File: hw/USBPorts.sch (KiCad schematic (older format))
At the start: 17 parts, among them J3 Conn_01x04, J4 USB_A, J5 Conn_01x04, J6 USB_A, J7 USB_A, J8 USB_A, U10 FSUSB31, U3 USB2517, U5 FSUSB31, U6 MIC2026-2BM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

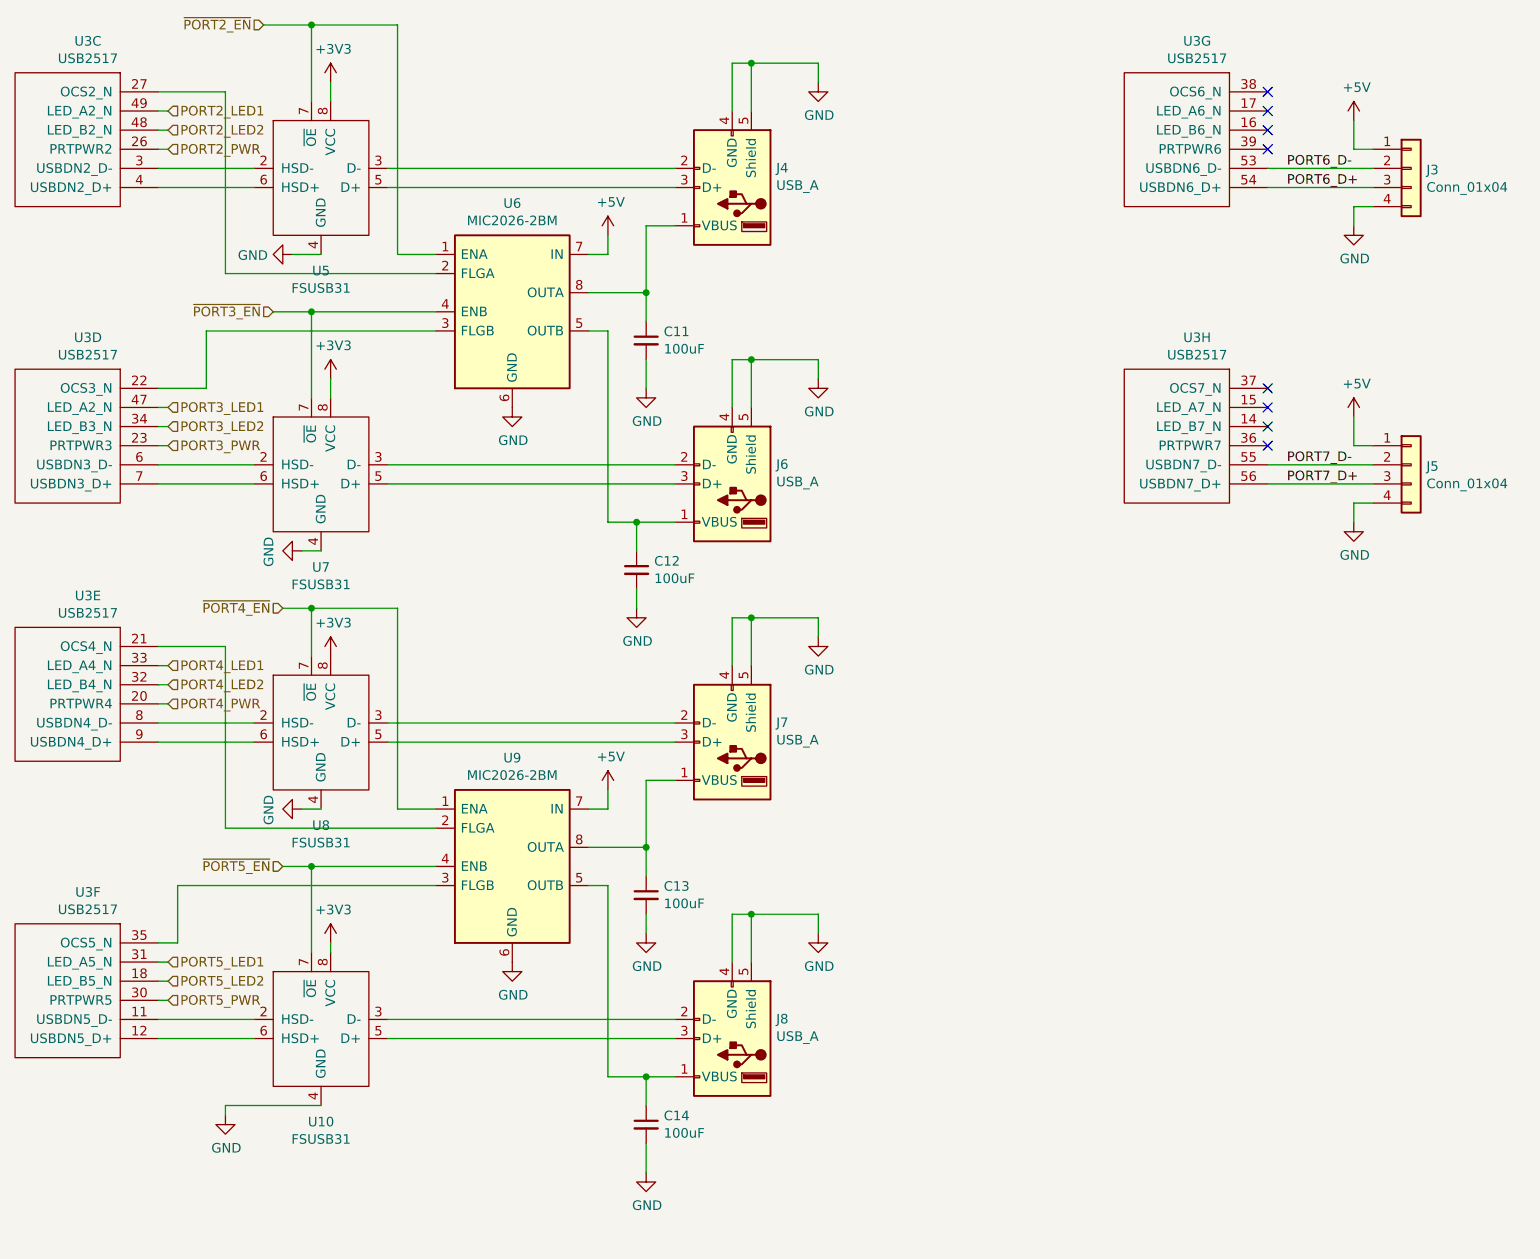
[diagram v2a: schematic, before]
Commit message: Add most footprints, switch to usb c
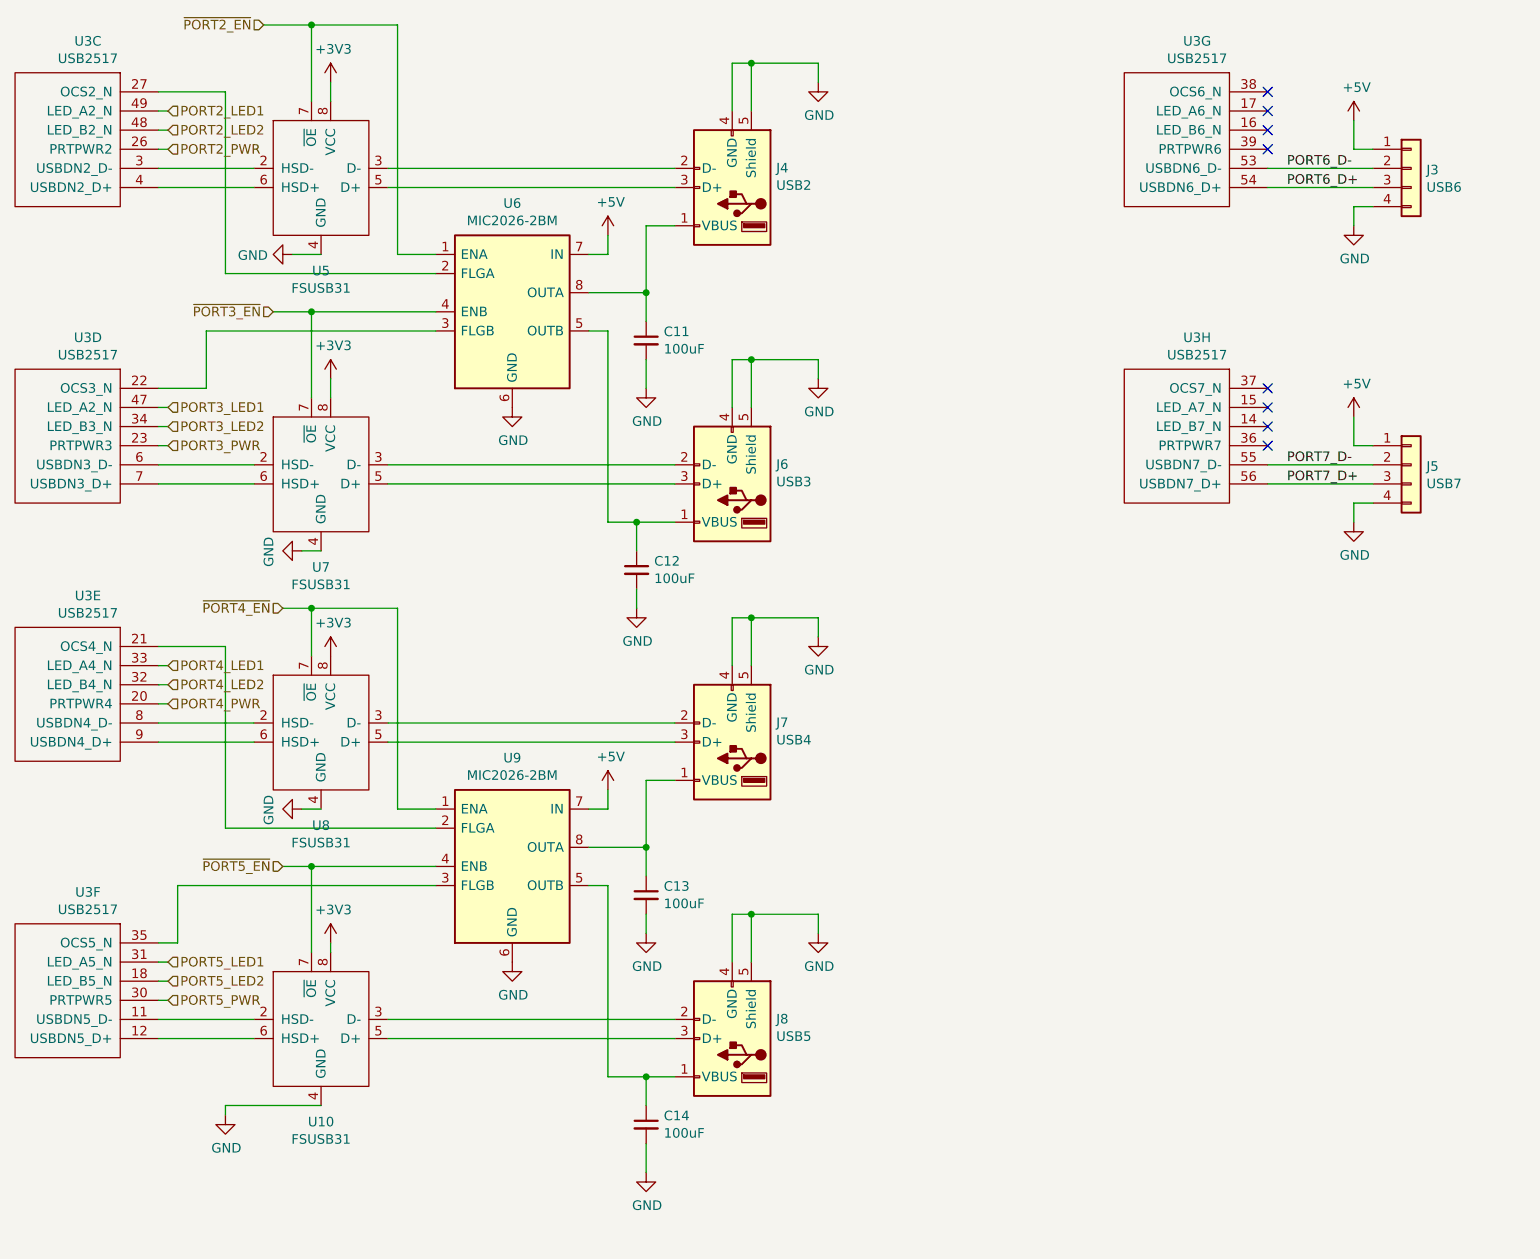
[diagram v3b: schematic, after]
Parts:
- C11, C12, C13, C14: footprint (none) -> Capacitor_SMD:C_0603_1608Metric
- J3: value Conn_01x04 -> USB6; footprint (none) -> Connector_PinHeader_2.54mm:PinHeader_1x04_P2.54mm_Vertical
- J4: value USB_A -> USB2; footprint (none) -> USB_A_Female_Vertical:USB_A_Female_Vertical
- J5: value Conn_01x04 -> USB7; footprint (none) -> Connector_PinHeader_2.54mm:PinHeader_1x04_P2.54mm_Vertical
- J6: value USB_A -> USB3; footprint (none) -> USB_A_Female_Vertical:USB_A_Female_Vertical
- J7: value USB_A -> USB4; footprint (none) -> USB_A_Female_Vertical:USB_A_Female_Vertical
- J8: value USB_A -> USB5; footprint (none) -> USB_A_Female_Vertical:USB_A_Female_Vertical
- U3: footprint (none) -> Package_DFN_QFN:QFN-64-1EP_9x9mm_P0.5mm_EP4.7x4.7mm_ThermalVias
- U6, U9: footprint (none) -> Package_SO:SOIC-8_3.9x4.9mm_P1.27mm
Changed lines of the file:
@@
 F 0 "U3" H 1531 2065 50  0000 C CNN
 F 1 "USB2517" H 1531 1974 50  0000 C CNN
-F 2 "" H 2550 3350 50  0001 C CNN
+F 2 "Package_DFN_QFN:QFN-64-1EP_9x9mm_P0.5mm_EP4.7x4.7mm_ThermalVias" H 2550 3350 50  0001 C CNN
 F 3 "" H 2550 3350 50  0001 C CNN
 	3    1450 1550
@@
 F 0 "U3" H 1531 3615 50  0000 C CNN
 F 1 "USB2517" H 1531 3524 50  0000 C CNN
-F 2 "" H 2550 4900 50  0001 C CNN
+F 2 "Package_DFN_QFN:QFN-64-1EP_9x9mm_P0.5mm_EP4.7x4.7mm_ThermalVias" H 2550 4900 50  0001 C CNN
 F 3 "" H 2550 4900 50  0001 C CNN
 	4    1450 3100
@@
 F 0 "U3" H 1531 4965 50  0000 C CNN
 F 1 "USB2517" H 1531 4874 50  0000 C CNN
-F 2 "" H 2550 6250 50  0001 C CNN
+F 2 "Package_DFN_QFN:QFN-64-1EP_9x9mm_P0.5mm_EP4.7x4.7mm_ThermalVias" H 2550 6250 50  0001 C CNN
 F 3 "" H 2550 6250 50  0001 C CNN
 	5    1450 4450
@@
 F 0 "U3" H 1531 6515 50  0000 C CNN
 F 1 "USB2517" H 1531 6424 50  0000 C CNN
-F 2 "" H 2550 7800 50  0001 C CNN
+F 2 "Package_DFN_QFN:QFN-64-1EP_9x9mm_P0.5mm_EP4.7x4.7mm_ThermalVias" H 2550 7800 50  0001 C CNN
 F 3 "" H 2550 7800 50  0001 C CNN
 	6    1450 6000
@@
 F 0 "U3" H 7331 2065 50  0000 C CNN
 F 1 "USB2517" H 7331 1974 50  0000 C CNN
-F 2 "" H 8350 3350 50  0001 C CNN
+F 2 "Package_DFN_QFN:QFN-64-1EP_9x9mm_P0.5mm_EP4.7x4.7mm_ThermalVias" H 8350 3350 50  0001 C CNN
 F 3 "" H 8350 3350 50  0001 C CNN
 	7    7250 1550
@@
 F 0 "U3" H 7331 3615 50  0000 C CNN
 F 1 "USB2517" H 7331 3524 50  0000 C CNN
-F 2 "" H 8350 4900 50  0001 C CNN
+F 2 "Package_DFN_QFN:QFN-64-1EP_9x9mm_P0.5mm_EP4.7x4.7mm_ThermalVias" H 8350 4900 50  0001 C CNN
 F 3 "" H 8350 4900 50  0001 C CNN
 	8    7250 3100
@@
 F 0 "U6" H 3750 3017 50  0000 C CNN
 F 1 "MIC2026-2BM" H 3750 2926 50  0000 C CNN
-F 2 "" H 3750 2450 50  0001 C CNN
+F 2 "Package_SO:SOIC-8_3.9x4.9mm_P1.27mm" H 3750 2450 50  0001 C CNN
 F 3 "http://www.micrel.com/_PDF/mic2026.pdf" H 3750 2450 50  0001 C CNN
 	1    3750 2450
@@
 P 4900 1800
 F 0 "J4" H 4670 1698 50  0000 R CNN
-F 1 "USB_A" H 4670 1789 50  0000 R CNN
-F 2 "" H 5050 1750 50  0001 C CNN
+F 1 "USB2" H 4670 1789 50  0000 R CNN
+F 2 "USB_A_Female_Vertical:USB_A_Female_Vertical" H 5050 1750 50  0001 C CNN
 F 3 " ~" H 5050 1750 50  0001 C CNN
 	1    4900 1800
@@
 P 4900 3350
 F 0 "J6" H 4670 3248 50  0000 R CNN
-F 1 "USB_A" H 4670 3339 50  0000 R CNN
-F 2 "" H 5050 3300 50  0001 C CNN
+F 1 "USB3" H 4670 3339 50  0000 R CNN
+F 2 "USB_A_Female_Vertical:USB_A_Female_Vertical" H 5050 3300 50  0001 C CNN
 F 3 " ~" H 5050 3300 50  0001 C CNN
 	1    4900 3350
@@
 F 0 "U9" H 3750 5917 50  0000 C CNN
 F 1 "MIC2026-2BM" H 3750 5826 50  0000 C CNN
-F 2 "" H 3750 5350 50  0001 C CNN
+F 2 "Package_SO:SOIC-8_3.9x4.9mm_P1.27mm" H 3750 5350 50  0001 C CNN
 F 3 "http://www.micrel.com/_PDF/mic2026.pdf" H 3750 5350 50  0001 C CNN
 	1    3750 5350
@@
 P 4900 4700
 F 0 "J7" H 4670 4598 50  0000 R CNN
-F 1 "USB_A" H 4670 4689 50  0000 R CNN
-F 2 "" H 5050 4650 50  0001 C CNN
+F 1 "USB4" H 4670 4689 50  0000 R CNN
+F 2 "USB_A_Female_Vertical:USB_A_Female_Vertical" H 5050 4650 50  0001 C CNN
 F 3 " ~" H 5050 4650 50  0001 C CNN
 	1    4900 4700
@@
 P 4900 6250
 F 0 "J8" H 4670 6148 50  0000 R CNN
-F 1 "USB_A" H 4670 6239 50  0000 R CNN
-F 2 "" H 5050 6200 50  0001 C CNN
+F 1 "USB5" H 4670 6239 50  0000 R CNN
+F 2 "USB_A_Female_Vertical:USB_A_Female_Vertical" H 5050 6200 50  0001 C CNN
 F 3 " ~" H 5050 6200 50  0001 C CNN
 	1    4900 6250
@@
 F 0 "C12" H 4492 3846 50  0000 L CNN
 F 1 "100uF" H 4492 3755 50  0000 L CNN
-F 2 "" H 4400 3800 50  0001 C CNN
+F 2 "Capacitor_SMD:C_0603_1608Metric" H 4400 3800 50  0001 C CNN
 F 3 "~" H 4400 3800 50  0001 C CNN
 	1    4400 3800
@@
 F 0 "C11" H 4542 2646 50  0000 L CNN
 F 1 "100uF" H 4542 2555 50  0000 L CNN
-F 2 "" H 4450 2600 50  0001 C CNN
+F 2 "Capacitor_SMD:C_0603_1608Metric" H 4450 2600 50  0001 C CNN
 F 3 "~" H 4450 2600 50  0001 C CNN
 	1    4450 2600
@@
 F 0 "C13" H 4542 5546 50  0000 L CNN
 F 1 "100uF" H 4542 5455 50  0000 L CNN
-F 2 "" H 4450 5500 50  0001 C CNN
+F 2 "Capacitor_SMD:C_0603_1608Metric" H 4450 5500 50  0001 C CNN
 F 3 "~" H 4450 5500 50  0001 C CNN
 	1    4450 5500
@@
 F 0 "C14" H 4542 6746 50  0000 L CNN
 F 1 "100uF" H 4542 6655 50  0000 L CNN
-F 2 "" H 4450 6700 50  0001 C CNN
+F 2 "Capacitor_SMD:C_0603_1608Metric" H 4450 6700 50  0001 C CNN
 F 3 "~" H 4450 6700 50  0001 C CNN
 	1    4450 6700
@@
 P 8450 1700
 F 0 "J3" H 8530 1692 50  0000 L CNN
-F 1 "Conn_01x04" H 8530 1601 50  0000 L CNN
-F 2 "" H 8450 1700 50  0001 C CNN
+F 1 "USB6" H 8530 1601 50  0000 L CNN
+F 2 "Connector_PinHeader_2.54mm:PinHeader_1x04_P2.54mm_Vertical" H 8450 1700 50  0001 C CNN
 F 3 "~" H 8450 1700 50  0001 C CNN
 	1    8450 1700
@@
 P 8450 3250
 F 0 "J5" H 8530 3242 50  0000 L CNN
-F 1 "Conn_01x04" H 8530 3151 50  0000 L CNN
-F 2 "" H 8450 3250 50  0001 C CNN
+F 1 "USB7" H 8530 3151 50  0000 L CNN
+F 2 "Connector_PinHeader_2.54mm:PinHeader_1x04_P2.54mm_Vertical" H 8450 3250 50  0001 C CNN
 F 3 "~" H 8450 3250 50  0001 C CNN
 	1    8450 3250

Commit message: Add footprints to everything else, except barrel jack
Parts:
- U10, U5, U7, U8: footprint (none) -> Package_US8:US-8
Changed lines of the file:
@@
 F 0 "U5" H 2750 1264 50  0000 C CNN
 F 1 "FSUSB31" H 2750 1173 50  0000 C CNN
-F 2 "" H 2850 1350 50  0001 C CNN
+F 2 "Package_US8:US-8" H 2850 1350 50  0001 C CNN
 F 3 "" H 2850 1350 50  0001 C CNN
 	1    2750 1750
@@
 F 0 "U7" H 2750 2814 50  0000 C CNN
 F 1 "FSUSB31" H 2750 2723 50  0000 C CNN
-F 2 "" H 2850 2900 50  0001 C CNN
+F 2 "Package_US8:US-8" H 2850 2900 50  0001 C CNN
 F 3 "" H 2850 2900 50  0001 C CNN
 	1    2750 3300
@@
 F 0 "U8" H 2750 4164 50  0000 C CNN
 F 1 "FSUSB31" H 2750 4073 50  0000 C CNN
-F 2 "" H 2850 4250 50  0001 C CNN
+F 2 "Package_US8:US-8" H 2850 4250 50  0001 C CNN
 F 3 "" H 2850 4250 50  0001 C CNN
 	1    2750 4650
@@
 F 0 "U10" H 2750 5714 50  0000 C CNN
 F 1 "FSUSB31" H 2750 5623 50  0000 C CNN
-F 2 "" H 2850 5800 50  0001 C CNN
+F 2 "Package_US8:US-8" H 2850 5800 50  0001 C CNN
 F 3 "" H 2850 5800 50  0001 C CNN
 	1    2750 6200

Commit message: Begin routing
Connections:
- net HUB2_D-: now reaches U3.3 (USBDN2_D-), U5.2 (HSD-)
- net USB2_D-: now reaches J4.2 (D-), U5.3 (D-)
- net USB2_D+: now reaches J4.3 (D+), U5.5 (D+)
- net HUB2_D+: now reaches U3.4 (USBDN2_D+), U5.6 (HSD+)
- net HUB3_D-: now reaches U3.6 (USBDN3_D-), U7.2 (HSD-)
- net USB3_D-: now reaches J6.2 (D-), U7.3 (D-)
- net USB_D+: now reaches J6.3 (D+), U7.5 (D+)
- net HUB3_D+: now reaches U3.7 (USBDN3_D+), U7.6 (HSD+)
- net HUB4_D-: now reaches U3.8 (USBDN4_D-), U8.2 (HSD-)
- net USB4_D-: now reaches J7.2 (D-), U8.3 (D-)
- net USB4_D+: now reaches J7.3 (D+), U8.5 (D+)
- net HUB4_D+: now reaches U3.9 (USBDN4_D+), U8.6 (HSD+)
- net HUB5_D-: now reaches U10.2 (HSD-), U3.11 (USBDN5_D-)
- net USB5_D-: now reaches J8.2 (D-), U10.3 (D-)
- net USB5_D+: now reaches J8.3 (D+), U10.5 (D+)
- net HUB5_D+: now reaches U10.6 (HSD+), U3.12 (USBDN5_D+)
- net USB3_VBUS: now reaches C12.1, J6.1 (VBUS)
- net USB3_VBUS: now also U6.8 (OUTA); no longer U6.5 (OUTB)
- net USB2_VBUS: now reaches C11.1, J4.1 (VBUS)
- net USB2_VBUS: now also U6.5 (OUTB); no longer U6.8 (OUTA)
- net USB5_VBUS: now reaches C14.1, J8.1 (VBUS)
- net USB5_VBUS: now also U9.8 (OUTA); no longer U9.5 (OUTB)
- net USB4_VBUS: now reaches C13.1, J7.1 (VBUS)
- net USB4_VBUS: now also U9.5 (OUTB); no longer U9.8 (OUTA)
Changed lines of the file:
@@
 $EndComp
-Wire Wire Line
-	4150 2350 4450 2350
-Wire Wire Line
-	4450 2350 4450 2000
 Wire Wire Line
 	4450 2000 4600 2000
@@
 	4600 3350 3100 3350
 Wire Wire Line
-	4250 3550 4250 2550
-Wire Wire Line
-	4250 2550 4150 2550
-Wire Wire Line
-	4250 3550 4400 3550
+	4350 3550 4400 3550
 $Comp
 L Power_Management:MIC2026-2BM U9
@@
 $EndComp
 Wire Wire Line
-	4150 5250 4450 5250
-Wire Wire Line
-	4450 5250 4450 4900
-Wire Wire Line
 	4450 4900 4600 4900
 $Comp
@@
 	4600 6250 3100 6250
 Wire Wire Line
-	4250 6450 4250 5450
-Wire Wire Line
-	4250 5450 4150 5450
-Wire Wire Line
-	4250 6450 4450 6450
+	4350 6450 4450 6450
 Wire Wire Line
 	5350 4050 5000 4050
@@
 Wire Wire Line
 	4450 2700 4450 2850
-Wire Wire Line
-	4450 2500 4450 2350
-Connection ~ 4450 2350
 $Comp
 L Device:C_Small C13
@@
 Wire Wire Line
 	4450 5700 4450 5600
-Wire Wire Line
-	4450 5400 4450 5250
-Connection ~ 4450 5250
 Text HLabel 2500 2450 0    50   Input ~ 0
 ~PORT3_EN~
@@
 	2700 5350 2550 5350
 Connection ~ 2700 5350
+Text Label 3250 3250 1    50   ~ 0
+USB3_D-
+Text Label 3250 3350 3    50   ~ 0
+USB_D+
+Text Label 3300 1700 1    50   ~ 0
+USB2_D-
+Text Label 3300 1800 3    50   ~ 0
+USB2_D+
+Text Label 3250 4600 1    50   ~ 0
+USB4_D-
+Text Label 3250 4700 3    50   ~ 0
+USB4_D+
+Text Label 3200 6250 3    50   ~ 0
+USB5_D+
+Text Label 3200 6150 1    50   ~ 0
+USB5_D-
+Text Label 1950 6150 0    50   ~ 0
+HUB5_D-
+Text Label 1950 6250 0    50   ~ 0
+HUB5_D+
+Text Label 1950 4600 0    50   ~ 0
+HUB4_D-
+Text Label 1950 4700 0    50   ~ 0
+HUB4_D+
+Text Label 1950 3350 0    50   ~ 0
+HUB3_D+
+Text Label 1950 3250 0    50   ~ 0
+HUB3_D-
+Text Label 1950 1700 0    50   ~ 0
+HUB2_D-
+Text Label 1950 1800 0    50   ~ 0
+HUB2_D+
+Text Label 4450 2250 0    50   ~ 0
+USB2_VBUS
+Text Label 4350 2700 3    50   ~ 0
+USB3_VBUS
+Text Label 4450 5150 0    50   ~ 0
+USB4_VBUS
+Text Label 4350 5950 1    50   ~ 0
+USB5_VBUS
+Wire Wire Line
+	4450 4900 4450 5200
+Wire Wire Line
+	4350 5250 4150 5250
+Wire Wire Line
+	4350 5250 4350 6450
+Wire Wire Line
+	4150 5450 4250 5450
+Wire Wire Line
+	4250 5450 4250 5200
+Wire Wire Line
+	4250 5200 4450 5200
+Connection ~ 4450 5200
+Wire Wire Line
+	4450 5200 4450 5400
+Wire Wire Line
+	4450 2000 4450 2300
+Wire Wire Line
+	4150 2350 4350 2350
+Wire Wire Line
+	4350 2350 4350 3550
+Wire Wire Line
+	4150 2550 4250 2550
+Wire Wire Line
+	4250 2550 4250 2300
+Wire Wire Line
+	4250 2300 4450 2300
+Connection ~ 4450 2300
+Wire Wire Line
+	4450 2300 4450 2500
 $EndSCHEMATC

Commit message: More placement, more issues
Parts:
- added D1, D3, D4, D5: G, LED_SMD:LED_0603_1608Metric, symbol Device:LED_Small
- added R15, R16, R17, R18: 2.2k, Resistor_SMD:R_0603_1608Metric, symbol Device:R_Small
- C11, C12, C13, C14: footprint Capacitor_SMD:C_0603_1608Metric -> Capacitor_SMD:CP_Elec_5x5.8
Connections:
- net GND: now also D1.1 (K), D3.1 (K), D4.1 (K), D5.1 (K)
- net USB2_VBUS: now also R17.2
- net USB3_VBUS: now also R15.1
- net USB4_VBUS: now also R18.2
- net USB5_VBUS: now also R16.1
- net ~PORT2_EN~: now also U6.4 (ENB); no longer U6.1 (ENA)
- net ~PORT3_EN~: now also U6.1 (ENA); no longer U6.4 (ENB)
- net ~PORT4_EN~: now also U9.4 (ENB); no longer U9.1 (ENA)
- net ~PORT5_EN~: now also U9.1 (ENA); no longer U9.4 (ENB)
- net USB2_OC: now reaches U3.27 (OCS2_N)
- net USB2_OC: now also U6.3 (FLGB); no longer U6.2 (FLGA)
- net USB3_OC: now reaches U3.22 (OCS3_N)
- net USB3_OC: now also U6.2 (FLGA); no longer U6.3 (FLGB)
- net USB4_OC: now reaches U3.21 (OCS4_N)
- net USB4_OC: now also U9.3 (FLGB); no longer U9.2 (FLGA)
- net USB5_OC: now reaches U3.35 (OCS5_N)
- net USB5_OC: now also U9.2 (FLGA); no longer U9.3 (FLGB)
- net PORT2_LED1: no longer names the net of U3.49 (LED_A2_N)
- net PORT2_LED2: no longer names the net of U3.48 (LED_B2_N)
- net PORT3_LED1: no longer names the net of U3.47 (LED_A2_N)
- net PORT3_LED2: no longer names the net of U3.34 (LED_B3_N)
- net PORT4_LED1: no longer names the net of U3.33 (LED_A4_N)
- net PORT4_LED2: no longer names the net of U3.32 (LED_B4_N)
- net PORT5_LED1: no longer names the net of U3.31 (LED_A5_N)
- net PORT5_LED2: no longer names the net of U3.18 (LED_B5_N)
- net USB_D+ renamed USB3_D+
- new net: D1.2 (A), R15.2
- new net: D4.2 (A), R17.1
- new net: D5.2 (A), R18.1
- new net: D3.2 (A), R16.2
- no-connect marks 8 -> 16
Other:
- moved on the sheet: C12, C14

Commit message: Final
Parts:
- added TP10: OCS5_N, TestPoint:TestPoint_Pad_D1.0mm, symbol Connector:TestPoint
- added TP7: OSC2_N, TestPoint:TestPoint_Pad_D1.0mm, symbol Connector:TestPoint
- added TP8: OCS3_N, TestPoint:TestPoint_Pad_D1.0mm, symbol Connector:TestPoint
- added TP9: OCS4_N, TestPoint:TestPoint_Pad_D1.0mm, symbol Connector:TestPoint
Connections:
- net USB2_OC: now also TP7.1
- net USB3_OC: now also TP8.1
- net USB4_OC: now also TP9.1
- net USB5_OC: now also TP10.1
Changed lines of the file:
@@
 	2700 4000 2550 4000
 Wire Wire Line
-	2250 5150 2250 4200
+	2250 5150 2250 4950
 Wire Wire Line
 	2250 4200 1900 4200
@@
 Wire Wire Line
 	2250 1300 2250 2350
+$Comp
+L Connector:TestPoint TP9
+U 1 1 5C1393AB
+P 2250 4950
+F 0 "TP9" V 2353 5024 50  0000 C CNN
+F 1 "OCS4_N" V 2354 5024 50  0001 C CNN
+F 2 "TestPoint:TestPoint_Pad_D1.0mm" H 2450 4950 50  0001 C CNN
+F 3 "~" H 2450 4950 50  0001 C CNN
+	1    2250 4950
+	0    -1   -1   0
+$EndComp
+Connection ~ 2250 4950
+Wire Wire Line
+	2250 4950 2250 4200
+$Comp
+L Connector:TestPoint TP10
+U 1 1 5C1395BF
+P 2000 5450
+F 0 "TP10" V 2103 5524 50  0000 C CNN
+F 1 "OCS5_N" V 2104 5524 50  0001 C CNN
+F 2 "TestPoint:TestPoint_Pad_D1.0mm" H 2200 5450 50  0001 C CNN
+F 3 "~" H 2200 5450 50  0001 C CNN
+	1    2000 5450
+	0    -1   -1   0
+$EndComp
+Connection ~ 2000 5450
+$Comp
+L Connector:TestPoint TP8
+U 1 1 5C13A00E
+P 2150 2550
+F 0 "TP8" V 2150 2738 50  0000 L CNN
+F 1 "OCS3_N" V 2254 2624 50  0001 C CNN
+F 2 "TestPoint:TestPoint_Pad_D1.0mm" H 2350 2550 50  0001 C CNN
+F 3 "~" H 2350 2550 50  0001 C CNN
+	1    2150 2550
+	0    -1   -1   0
+$EndComp
+Connection ~ 2150 2550
+$Comp
+L Connector:TestPoint TP7
+U 1 1 5C13A268
+P 2250 1300
+F 0 "TP7" H 2308 1374 50  0000 L CNN
+F 1 "OSC2_N" V 2354 1374 50  0001 C CNN
+F 2 "TestPoint:TestPoint_Pad_D1.0mm" H 2450 1300 50  0001 C CNN
+F 3 "~" H 2450 1300 50  0001 C CNN
+	1    2250 1300
+	1    0    0    -1
+$EndComp
+Connection ~ 2250 1300
 $EndSCHEMATC
